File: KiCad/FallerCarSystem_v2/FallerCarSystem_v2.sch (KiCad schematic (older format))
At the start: 77 parts, among them J1 Conn_01x01_Male, J10 Conn_01x01_Male, J11 Conn_01x01_Male, J12 Conn_01x01_Male, J13 Conn_01x01_Male, J14 Conn_01x01_Male, J15 Conn_01x01_Male, J16 Conn_01x01_Male, J17 Conn_01x01_Male, J18 Conn_01x01_Male, J19 Conn_01x01_Male, J2 Conn_01x01_Male, J20 Conn_01x01_Male, J21 Conn_01x01_Male, J22 Conn_01x01_Male, J23 Conn_01x01_Male, J24 Conn_01x01_Male, J25 Conn_01x01_Male, J26 Conn_01x01_Male, J27 Conn_01x01_Male, J28 Conn_01x01_Male, J29 Conn_01x01_Male, J3 Conn_01x01_Male, J30 Conn_01x01_Male, J31 Conn_01x01_Male, J32 Conn_01x01_Male, J33 Conn_01x01_Male, J34 Conn_01x01_Male, J35 Conn_01x01_Male, J36 Conn_01x01_Male, J37 Conn_01x01_Male, J38 Conn_01x01_Male, J4 Conn_01x01_Male, J5 Conn_01x01_Male, J6 Conn_01x01_Male, J7 Conn_01x01_Male, J8 Conn_01x01_Male, J9 Conn_01x01_Male, U1 PIC16F15345-I_GZ-MCU_Microchi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, U2 MCP73871-2AA, U3 MCP1725-ADJE_MC_DFN-8-Regulat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

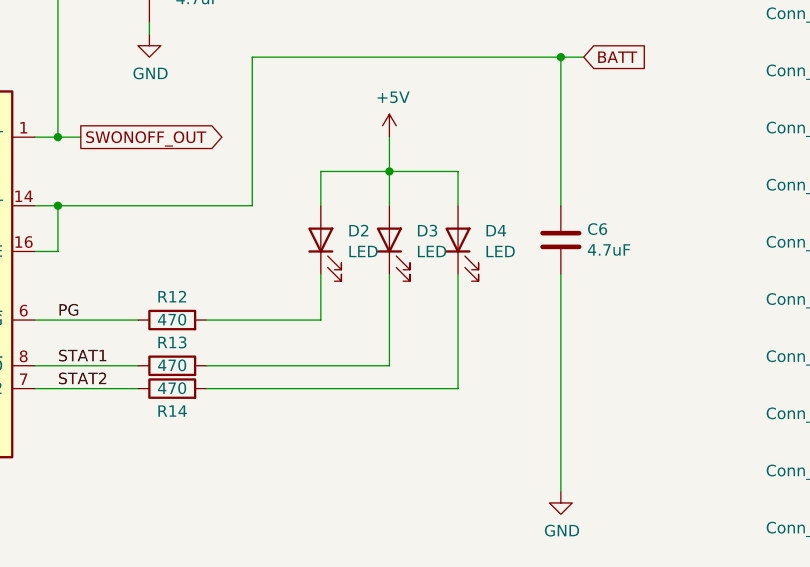
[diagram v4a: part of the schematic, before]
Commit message: added led color
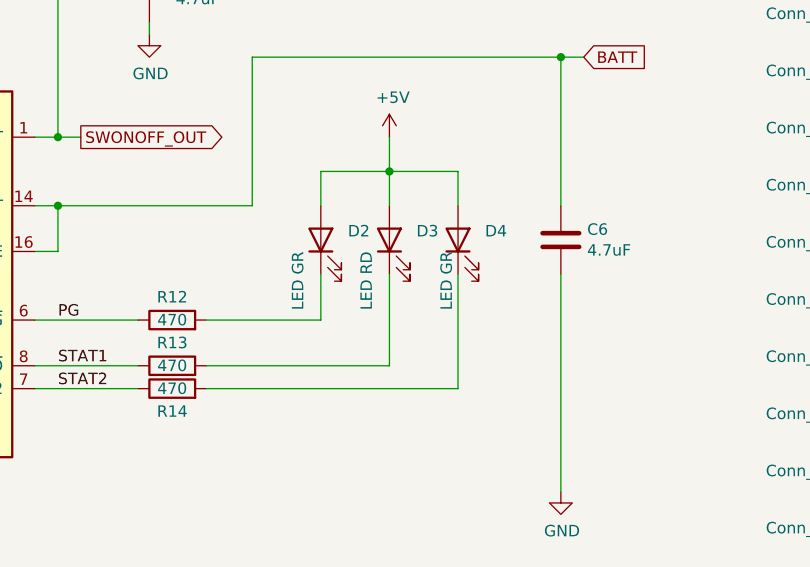
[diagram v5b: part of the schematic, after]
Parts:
- D2, D4: value LED -> LED GR
- D3: value LED -> LED RD
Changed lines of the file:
@@
 P 7250 2150
 F 0 "D3" V 7289 2032 50  0000 R CNN
-F 1 "LED" V 7198 2032 50  0000 R CNN
+F 1 "LED RD" H 7200 2250 50  0000 R CNN
 F 2 "LED_SMD:LED_0402_1005Metric" H 7250 2150 50  0001 C CNN
 F 3 "~" H 7250 2150 50  0001 C CNN
@@
 P 6950 2150
 F 0 "D2" V 6989 2032 50  0000 R CNN
-F 1 "LED" V 6898 2032 50  0000 R CNN
+F 1 "LED GR" H 6900 2250 50  0000 R CNN
 F 2 "LED_SMD:LED_0402_1005Metric" H 6950 2150 50  0001 C CNN
 F 3 "~" H 6950 2150 50  0001 C CNN
@@
 P 7550 2150
 F 0 "D4" V 7589 2032 50  0000 R CNN
-F 1 "LED" V 7498 2032 50  0000 R CNN
+F 1 "LED GR" H 7500 2200 50  0000 R CNN
 F 2 "LED_SMD:LED_0402_1005Metric" H 7550 2150 50  0001 C CNN
 F 3 "~" H 7550 2150 50  0001 C CNN

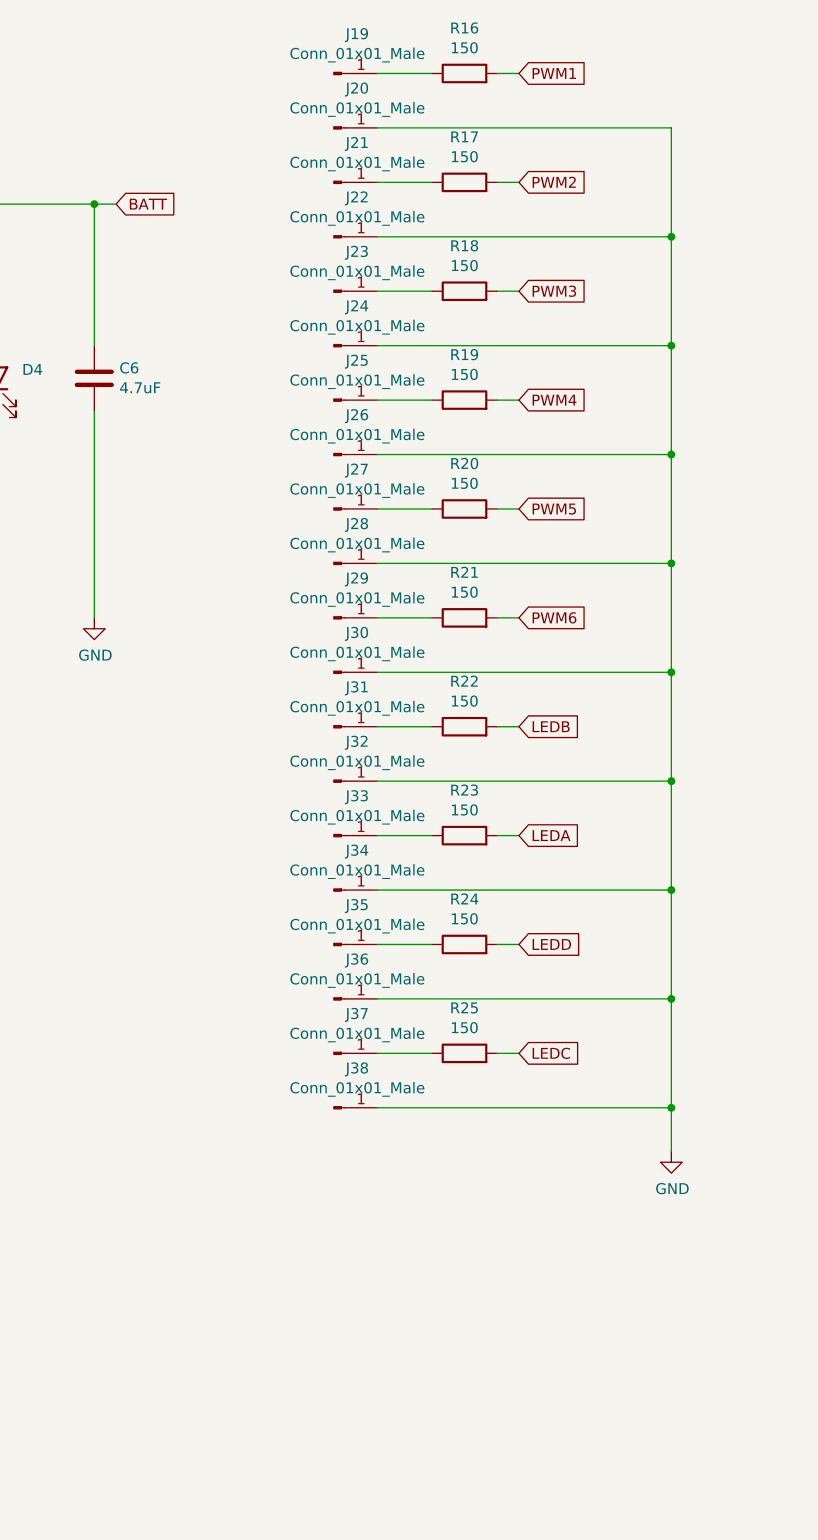
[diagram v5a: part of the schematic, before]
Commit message: Added some info to the schematic
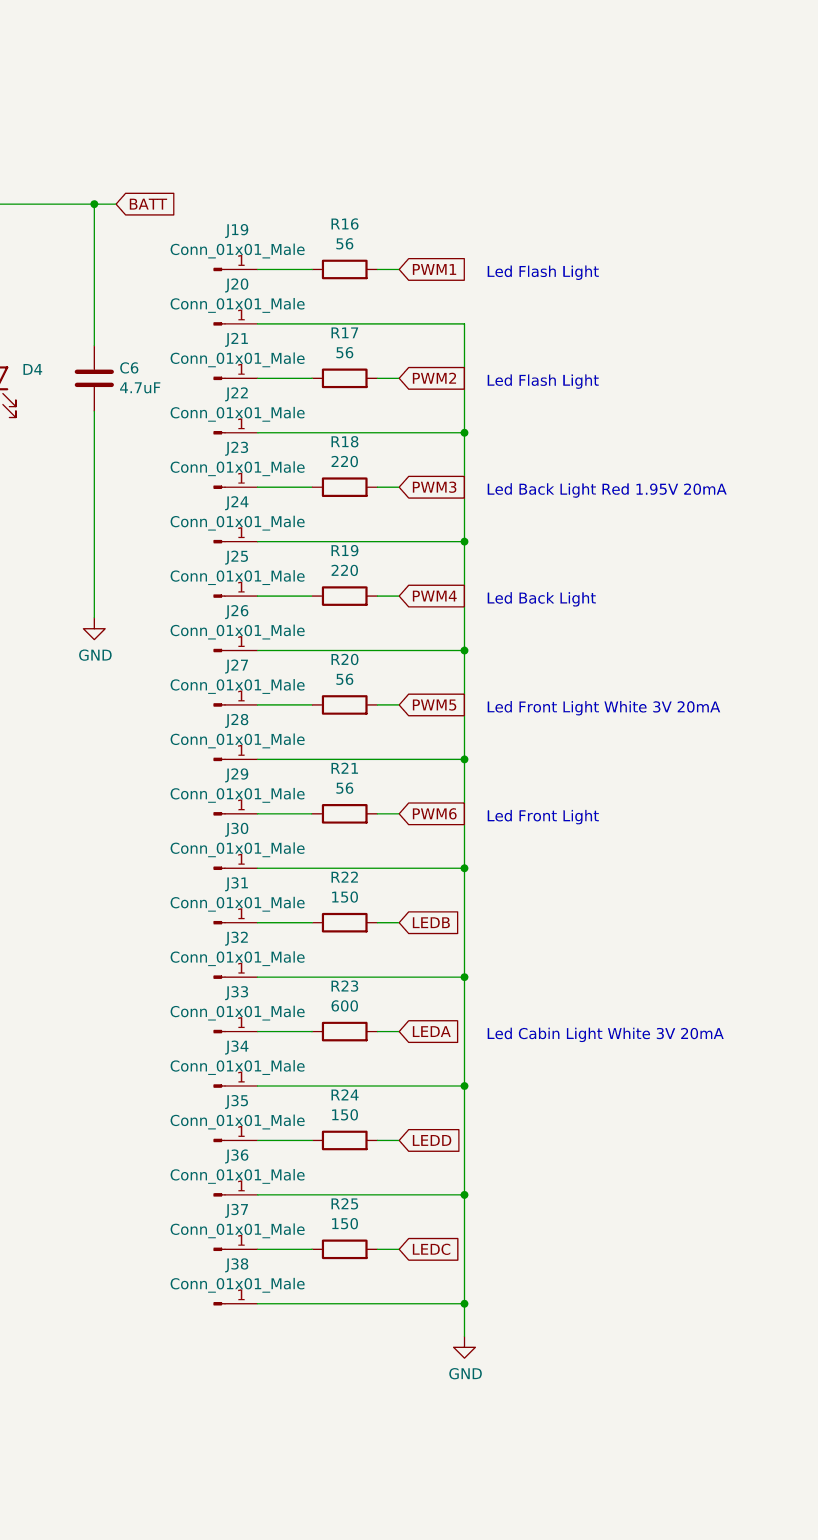
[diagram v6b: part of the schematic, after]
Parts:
- R16, R17, R20, R21: value 150 -> 56
- R18, R19: value 150 -> 220
- R23: value 150 -> 600
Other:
- note added: "Led Back Light"
- note added: "Led Back Light Red 1.95V 20mA"
- note added: "Led Cabin Light White 3V 20mA"
- note added: "Led Flash Light"
- note added: "Led Front Light"
- note added: "Led Front Light White 3V 20mA"
- moved on the sheet: J19, J20, J21, J22, J23, J24, J25, J26, J27, J28, J29, J30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
